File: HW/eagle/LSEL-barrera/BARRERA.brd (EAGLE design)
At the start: 26.7 x 17.1 mm, 8 parts

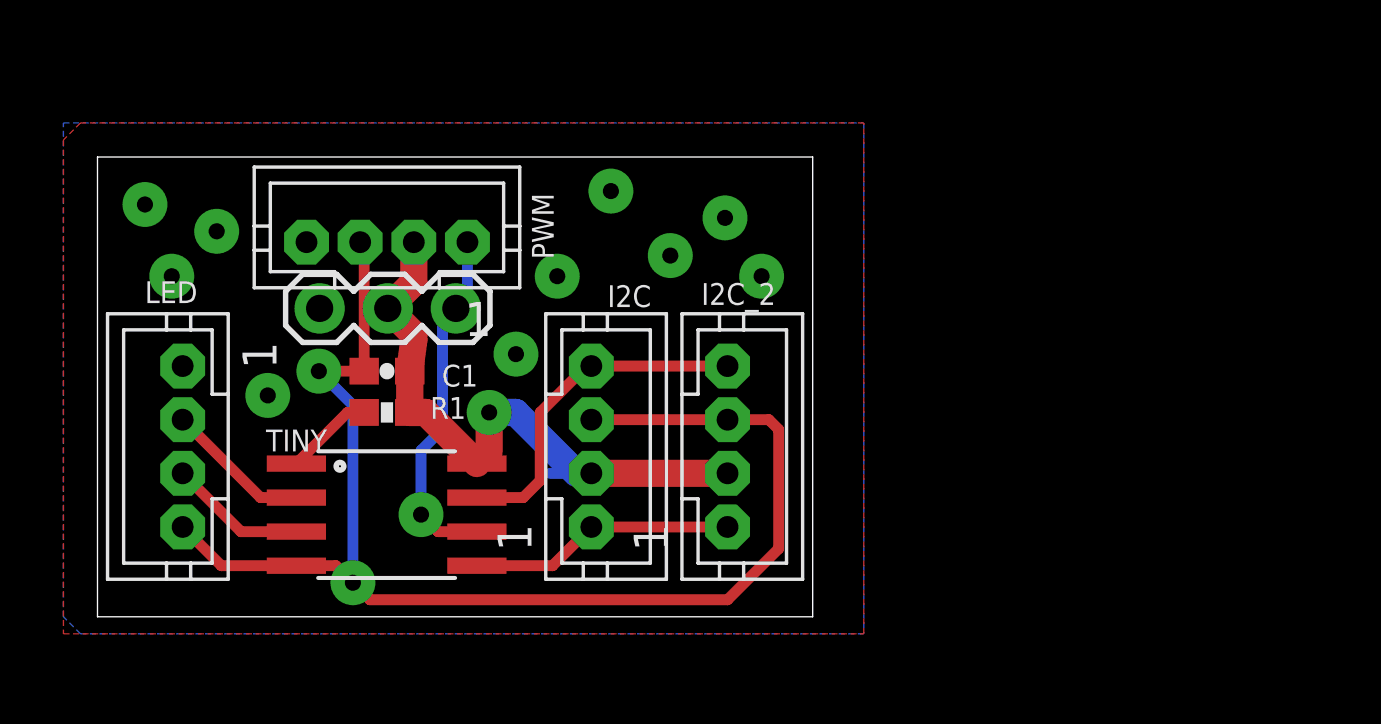
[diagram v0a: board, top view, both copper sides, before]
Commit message: Barrera RJ changed
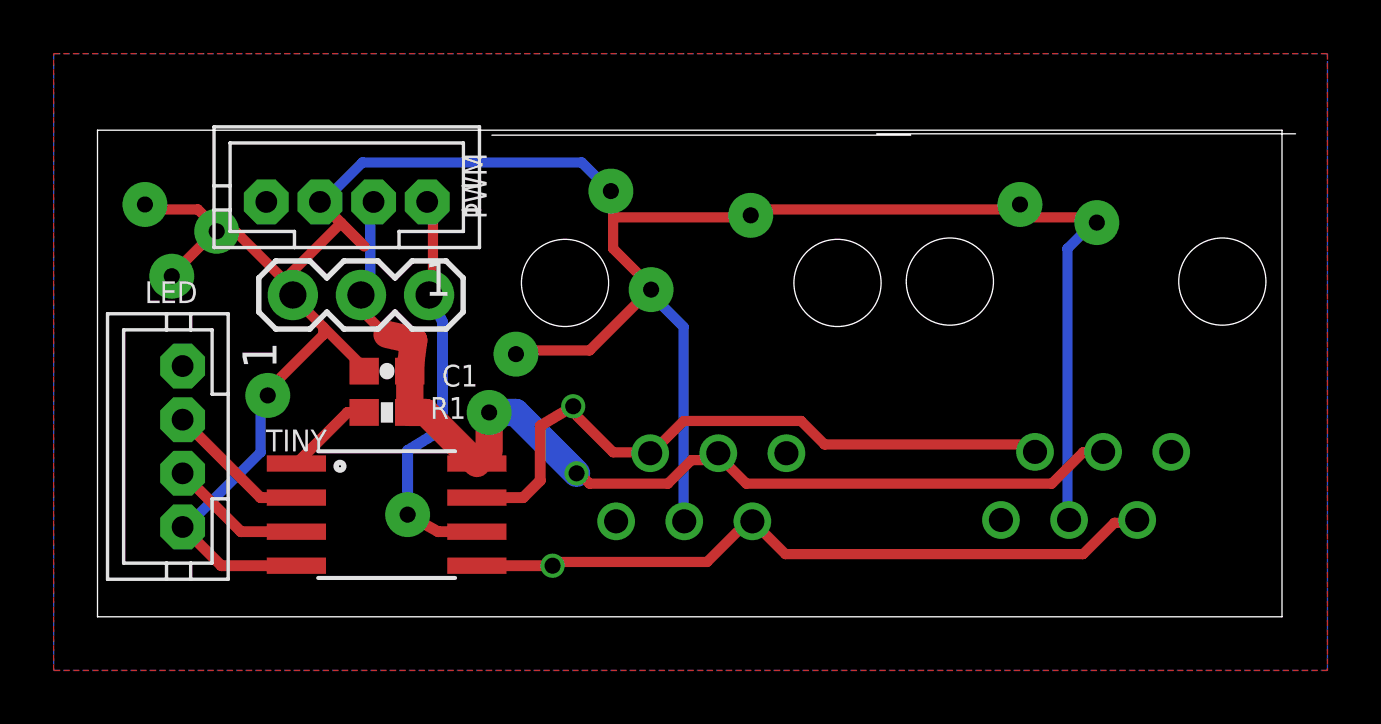
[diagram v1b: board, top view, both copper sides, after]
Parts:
- removed I2C_2: (no value), jst-ph:JST-PH4
- added I2C1: RJ11-2L-B, con-tycoelectronics:RJ11-NO_SHIELD
- I2C: value (none) -> RJ11-2L-B; device jst-ph:JST-PH4 -> con-tycoelectronics:RJ11-NO_SHIELD
- moved I2C 7.35 mm to (23.1, 12.4), flipped to the bottom, turned to 180 degrees
- moved PWM 2.12 mm to (9.93, 15.5)
- moved JP1 1.12 mm to (13.0, 12.0)
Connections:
- net GND: now also I2C1.3; no longer I2C_2.3
- net SCL: now also I2C.2, I2C1.2; no longer I2C.4, I2C_2.4
- net SDA: now also I2C.5, I2C1.5; no longer I2C.1, I2C_2.1
- net VCC: now also I2C.4, I2C1.4; no longer I2C.2, I2C_2.2
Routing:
- net GND: track 50.7 -> 95.6 mm, vias 12 -> 10
- net VCC: track 24.0 -> 40.7 mm, vias 1 -> 2
- net SDA: track 9.95 -> 26.3 mm, vias 0 -> 1
- net SCL: track 12.9 -> 25.1 mm, vias 0 -> 1
- net PWM: track 13.2 -> 15.4 mm
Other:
- board size 26.7 x 17.1 mm -> 44.2 x 18.1 mm
